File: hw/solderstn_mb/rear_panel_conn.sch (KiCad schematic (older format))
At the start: 15 parts, among them J1201 Conn_02x05_Odd_Even, J1202 USB_B-TE_1734346-1, J1203 DB9_Male_MountingHoles, J1204 USB_A-CUI-UJ2-AH-1-SMT, U1201 USBLC6-2SC6, U1202 74LVC2G17gw, U1203 USBLC6-2SC6

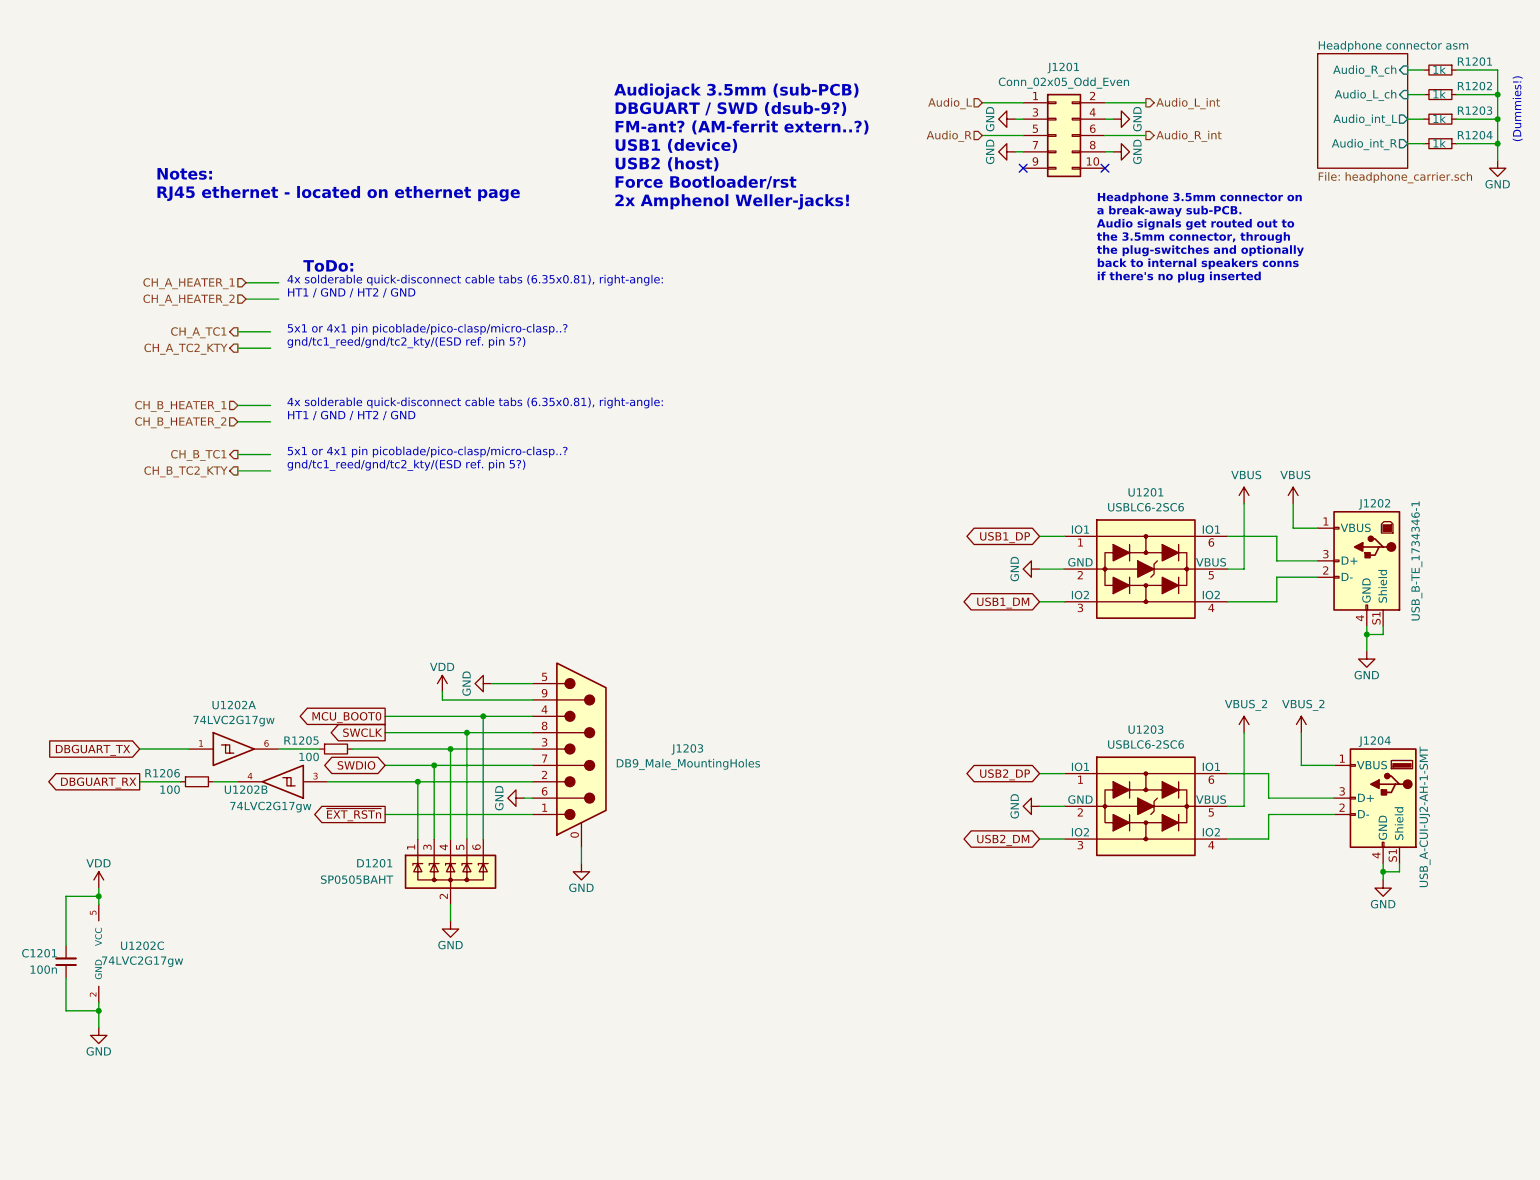
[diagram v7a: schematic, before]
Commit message: Add 12V DC-out (Molex Nano-Fit 1x02) and SMA in back-panel, for FM antenna & ext. ant.amp. Updated Dsub9 conn to correct component & placement on MB.
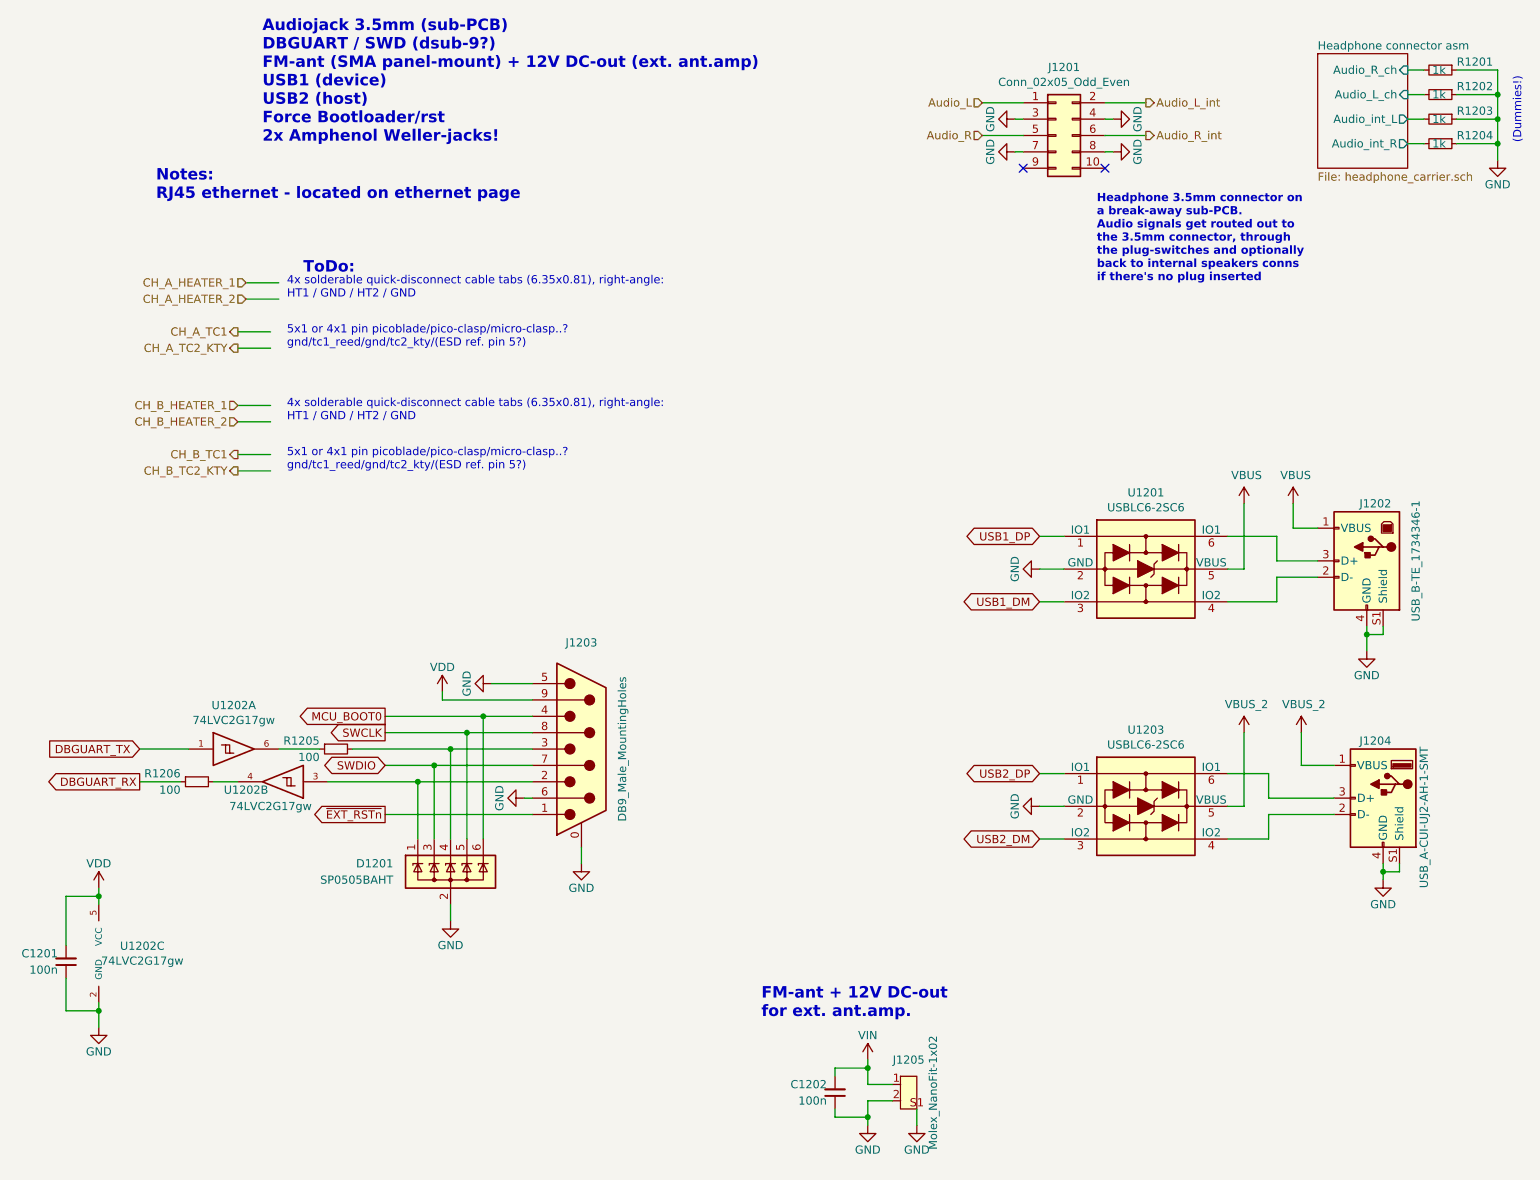
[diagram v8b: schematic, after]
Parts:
- added C1202: 100n, Capacitor_SMD:C_0603_1608Metric, symbol Device:C_Small
- added J1205: Molex_NanoFit-1x02, customlib_mj_fp:Molex_NanoFit_105430-1102_1x02_P2.50mm_Horizontal, symbol customlib_mj:Molex_NanoFit-1x02
- J1203: footprint Connector_Dsub:DSUB-9_Male_Horizontal_P2.77x2.84mm_EdgePinOffset9.90mm_Housed_MountingHolesOffset11.32mm -> customlib_mj_fp:DSub9-Kycon_K22X-EP9P-N
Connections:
- net labels added: VIN
- wire segments 96 -> 107
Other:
- note added: "Audiojack 3.5mm (sub-PCB)\nDBGUART / SWD (dsub-9?)\nFM-ant (SMA panel-mount) + 12V DC-out (ext. ant.amp)\nUSB1 (device)\nUSB2 (host)\nForce Bootloader/rst\n2x Amphenol Weller-jacks!"
- note added: "FM-ant + 12V DC-out\nfor ext. ant.amp."
- note removed: "Audiojack 3.5mm (sub-PCB)\nDBGUART / SWD (dsub-9?)\nFM-ant? (AM-ferrit extern..?)\nUSB1 (device)\nUSB2 (host)\nForce Bootloader/rst\n2x Amphenol Weller-jacks!"
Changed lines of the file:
@@
 Wire Wire Line
 	2250 3500 2450 3500
-Text Notes 4550 1900 0    70   ~ 14
-Audiojack 3.5mm (sub-PCB)\nDBGUART / SWD (dsub-9?)\nFM-ant? (AM-ferrit extern..?)\nUSB1 (device)\nUSB2 (host)\nForce Bootloader/rst\n2x Amphenol Weller-jacks!
+Text Notes 2400 1500 0    70   ~ 14
+Audiojack 3.5mm (sub-PCB)\nDBGUART / SWD (dsub-9?)\nFM-ant (SMA panel-mount) + 12V DC-out (ext. ant.amp)\nUSB1 (device)\nUSB2 (host)\nForce Bootloader/rst\n2x Amphenol Weller-jacks!
 Text GLabel 3150 5600 0    50   Output ~ 0
 ~EXT_RSTn~
@@
 U 1 1 5F3A1DC2
 P 4350 5200
-F 0 "J1203" H 5002 5202 50  0000 C CNN
-F 1 "DB9_Male_MountingHoles" H 5002 5111 50  0000 C CNN
-F 2 "Connector_Dsub:DSUB-9_Male_Horizontal_P2.77x2.84mm_EdgePinOffset9.90mm_Housed_MountingHolesOffset11.32mm" H 4350 5200 50  0001 C CNN
+F 0 "J1203" H 4350 5850 50  0000 C CNN
+F 1 "DB9_Male_MountingHoles" V 4600 5200 50  0000 C CNN
+F 2 "customlib_mj_fp:DSub9-Kycon_K22X-EP9P-N" H 4350 5200 50  0001 C CNN
 F 3 " ~" H 4350 5200 50  0001 C CNN
 	1    4350 5200
@@
 	-1   0    0    -1
 $EndComp
+$Comp
+L customlib_mj:Molex_NanoFit-1x02 J1205
+U 1 1 5F7E9080
+P 6350 7300
+F 0 "J1205" H 6350 7500 50  0000 C CNN
+F 1 "Molex_NanoFit-1x02" V 6500 7300 50  0000 C CNN
+F 2 "customlib_mj_fp:Molex_NanoFit_105430-1102_1x02_P2.50mm_Horizontal" H 6350 7300 50  0001 C CNN
+F 3 "https://www.molex.com/molex/products/part-detail/pcb_headers/1054301102" H 6350 7300 50  0001 C CNN
+	1    6350 7300
+	1    0    0    -1
+$EndComp
+$Comp
+L power:GND #PWR01222
+U 1 1 5F7EA1DC
+P 6100 7500
+F 0 "#PWR01222" H 6100 7250 50  0001 C CNN
+F 1 "GND" H 6100 7350 50  0000 C CNN
+F 2 "" H 6100 7500 50  0001 C CNN
+F 3 "" H 6100 7500 50  0001 C CNN
+	1    6100 7500
+	1    0    0    -1
+$EndComp
+Wire Wire Line
+	6100 7500 6100 7450
+Wire Wire Line
+	6100 7350 6250 7350
+$Comp
+L customlib_mj:VIN #PWR01221
+U 1 1 5F7FDE13
+P 6100 7100
+F 0 "#PWR01221" H 6100 6950 50  0001 C CNN
+F 1 "VIN" H 6100 7250 50  0000 C CNN
+F 2 "" H 6100 7100 50  0001 C CNN
+F 3 "" H 6100 7100 50  0001 C CNN
+	1    6100 7100
+	1    0    0    -1
+$EndComp
+Wire Wire Line
+	6250 7250 6100 7250
+Wire Wire Line
+	6100 7250 6100 7150
+$Comp
+L Device:C_Small C1202
+U 1 1 5F80162E
+P 5900 7300
+F 0 "C1202" H 5950 7250 50  0000 L CNN
+F 1 "100n" H 5950 7350 50  0000 L CNN
+F 2 "Capacitor_SMD:C_0603_1608Metric" H 5900 7300 50  0001 C CNN
+F 3 "~" H 5900 7300 50  0001 C CNN
+	1    5900 7300
+	-1   0    0    1
+$EndComp
+Wire Wire Line
+	5900 7200 5900 7150
+Wire Wire Line
+	5900 7150 6100 7150
+Connection ~ 6100 7150
+Wire Wire Line
+	6100 7150 6100 7100
+Wire Wire Line
+	5900 7400 5900 7450
+Wire Wire Line
+	5900 7450 6100 7450
+Connection ~ 6100 7450
+Wire Wire Line
+	6100 7450 6100 7350
+Text Notes 5450 6850 0    70   ~ 14
+FM-ant + 12V DC-out\nfor ext. ant.amp.
+$Comp
+L power:GND #PWR?
+U 1 1 5F8779FF
+P 6400 7500
+F 0 "#PWR?" H 6400 7250 50  0001 C CNN
+F 1 "GND" H 6400 7350 50  0000 C CNN
+F 2 "" H 6400 7500 50  0001 C CNN
+F 3 "" H 6400 7500 50  0001 C CNN
+	1    6400 7500
+	1    0    0    -1
+$EndComp
+Wire Wire Line
+	6400 7500 6400 7400
 $EndSCHEMATC
